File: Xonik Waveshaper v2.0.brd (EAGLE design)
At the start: 63.5 x 28.4 mm, 89 parts, among them IC1 TL074D, IC2 TL074D, IC3 TL074D, IC4 TL072D, IC5 4013D, T1 2n3904

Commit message: Vector xonik logo
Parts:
- moved 10 0.06 mm to (4.45, 8.89)
- moved 11 0.06 mm to (1.91, 8.89)
- moved 12 0.06 mm to (15.9, 21.3)
- moved 14 0.06 mm to (15.9, 19.0)
- moved 23 0.06 mm to (19.7, 8.89)
- moved 24 0.06 mm to (22.2, 8.89)
- moved 27 0.06 mm to (56.3, 8.89)
- moved 28 0.06 mm to (53.7, 8.89)
- moved 30 0.06 mm to (51.2, 8.89)
- moved 39 0.06 mm to (29.3, 19.9)
- moved 4 0.06 mm to (12.1, 8.89)
- moved 41 0.06 mm to (34.4, 19.9)
- moved 45 0.06 mm to (35.9, 8.89)
- moved 46 0.06 mm to (38.5, 8.89)
- moved 48 0.06 mm to (46.1, 8.89)
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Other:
- board size 63.5 x 28.4 mm -> 63.5 x 28.5 mm
- board text added: "Waveshaper"
- board text removed: "XWS"

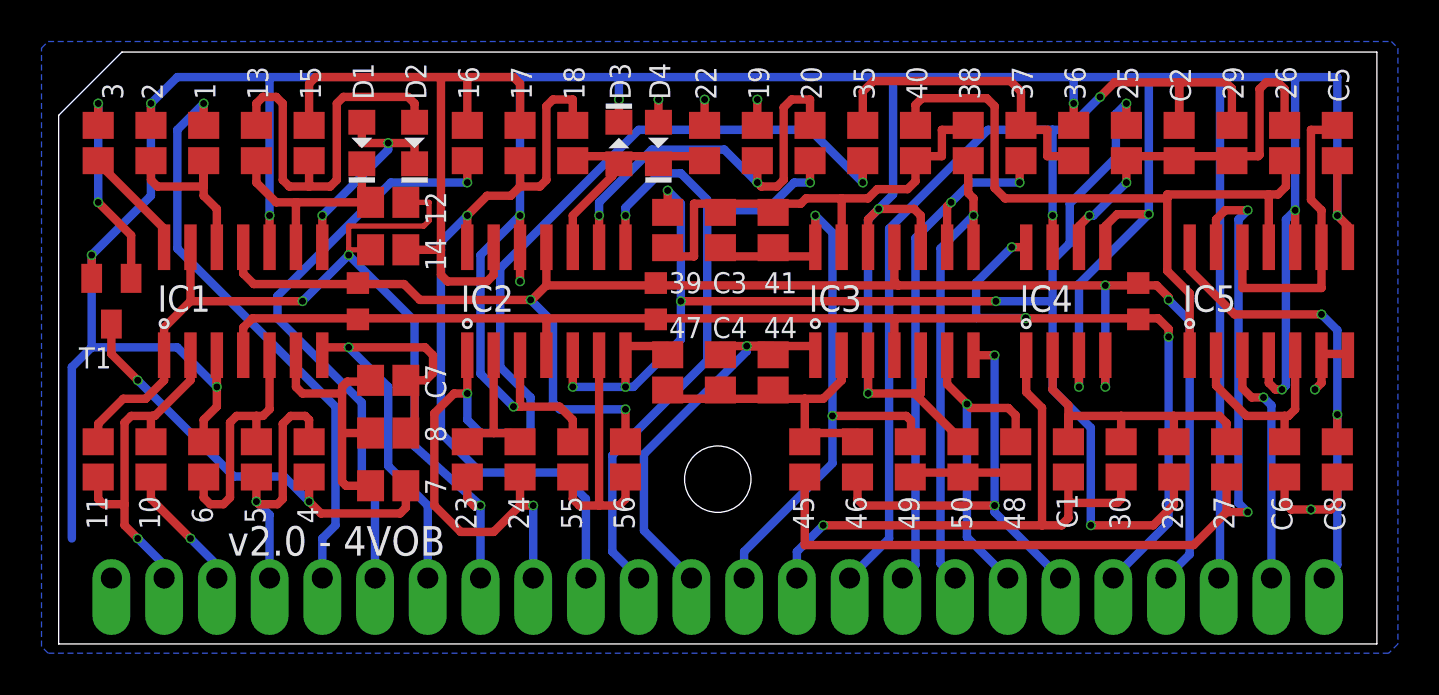
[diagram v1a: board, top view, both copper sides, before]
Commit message: Better clearance around bypass caps
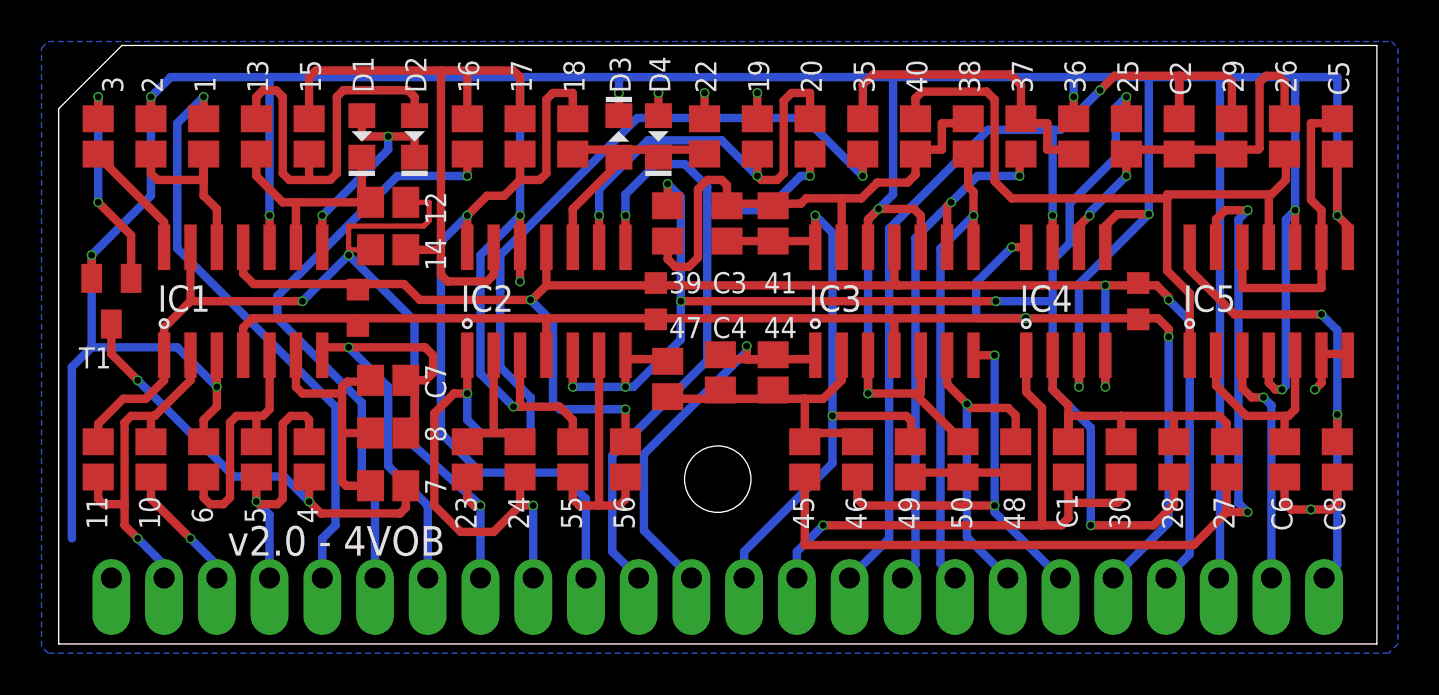
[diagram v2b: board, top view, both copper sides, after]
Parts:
- moved C3 0.45 mm to (32.2, 20.3)
- moved 1 0.32 mm to (6.99, 24.4)
- moved 13 0.32 mm to (9.53, 24.4)
- moved 15 0.32 mm to (12.1, 24.4)
- moved 16 0.32 mm to (19.7, 24.4)
- moved 17 0.32 mm to (22.2, 24.4)
- moved 18 0.32 mm to (24.8, 24.4)
- moved 19 0.32 mm to (33.7, 24.4)
- moved 2 0.32 mm to (4.45, 24.4)
- moved 20 0.32 mm to (36.2, 24.4)
- moved 22 0.32 mm to (31.1, 24.4)
- moved 25 0.32 mm to (51.4, 24.4)
- moved 26 0.32 mm to (59.1, 24.4)
- moved 29 0.32 mm to (56.5, 24.4)
- moved 3 0.32 mm to (1.91, 24.4)
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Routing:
- net N$26: track 23.8 -> 25.9 mm
- net N$27: track 32.2 -> 30.5 mm
- net N$30: track 22.7 -> 21.3 mm
- net N$40: track 34.3 -> 35.5 mm
- net N$16: track 54.4 -> 55.1 mm
- net N$36: track 20.4 -> 21.0 mm
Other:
- board size 63.5 x 28.5 mm -> 63.5 x 28.8 mm
